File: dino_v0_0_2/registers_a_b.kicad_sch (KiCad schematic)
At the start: 21 parts, among them U31 74LS373, U32 74LS373, U33 74LS373, U35 74LS373, U41 74LS245, U42 74LS245, U43 74LS245, U44 74LS245, U5 74LS08, U57 74LS02

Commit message: feat(kicad): footprints, power sheet, global labels, PCB draft
Every symbol gets a stock THT footprint (plain DIP, no sockets, so the
3D render shows ICs). New Power sheet: 24-pin ATX header for a picoPSU,
rails +5V/+3.3V/+12V/-12V/GND only; no -5V exists on any ATX unit since
2003, none drawn. PS_ON# on a 2-pin header.

Cross-sheet labels become global labels. KiCad joined nothing between
sheets before: 122 base names were split per sheet, ERC saw 90 undriven
inputs whose driver sat one sheet away, and the PCB ratsnest stopped at
every sheet boundary. Proof: KiCad's netlist after equals a name-join of
its netlist before plus the 15 CW alias pairs, pin for pin.

kicad_contracts took a node's sheet from the net name's /Sheet/ prefix;
global nets have none, so it emitted an empty contracts doc. Sheet now
comes from the component's own path; the doc regenerates with zero diff.

ERC 477 -> 2. Real fixes: ROM I/O pins input -> tri_state, '382 GND pin
power_out -> power_in, four orphan symbols rehomed to project lib `dino`,
one stub wire. 133 by-design warnings excluded by uuid ('245 readback on
counter Q, alias stubs, probe-point labels); the two left are bus
signals the peripheral bus sheet will consume.

PCB draft: 198 footprints placed per sheet, all pads netted, no tracks.

Co-Authored-By: Claude Fable 5.1 <noreply@anthropic.com>
Claude-Session: https://claude.ai/code/session_018irreFHb1xEykW5kCD26ow
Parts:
- C38, C39, C40, C41, C42, C43, C44, C45, C46, C47, C64: footprint (none) -> Capacitor_THT:C_Disc_D5.0mm_W2.5mm_P2.50mm
- U31, U32, U33, U35, U41, U42, U43, U44: footprint (none) -> Package_DIP:DIP-20_W7.62mm
- U5, U57: footprint (none) -> Package_DIP:DIP-14_W7.62mm

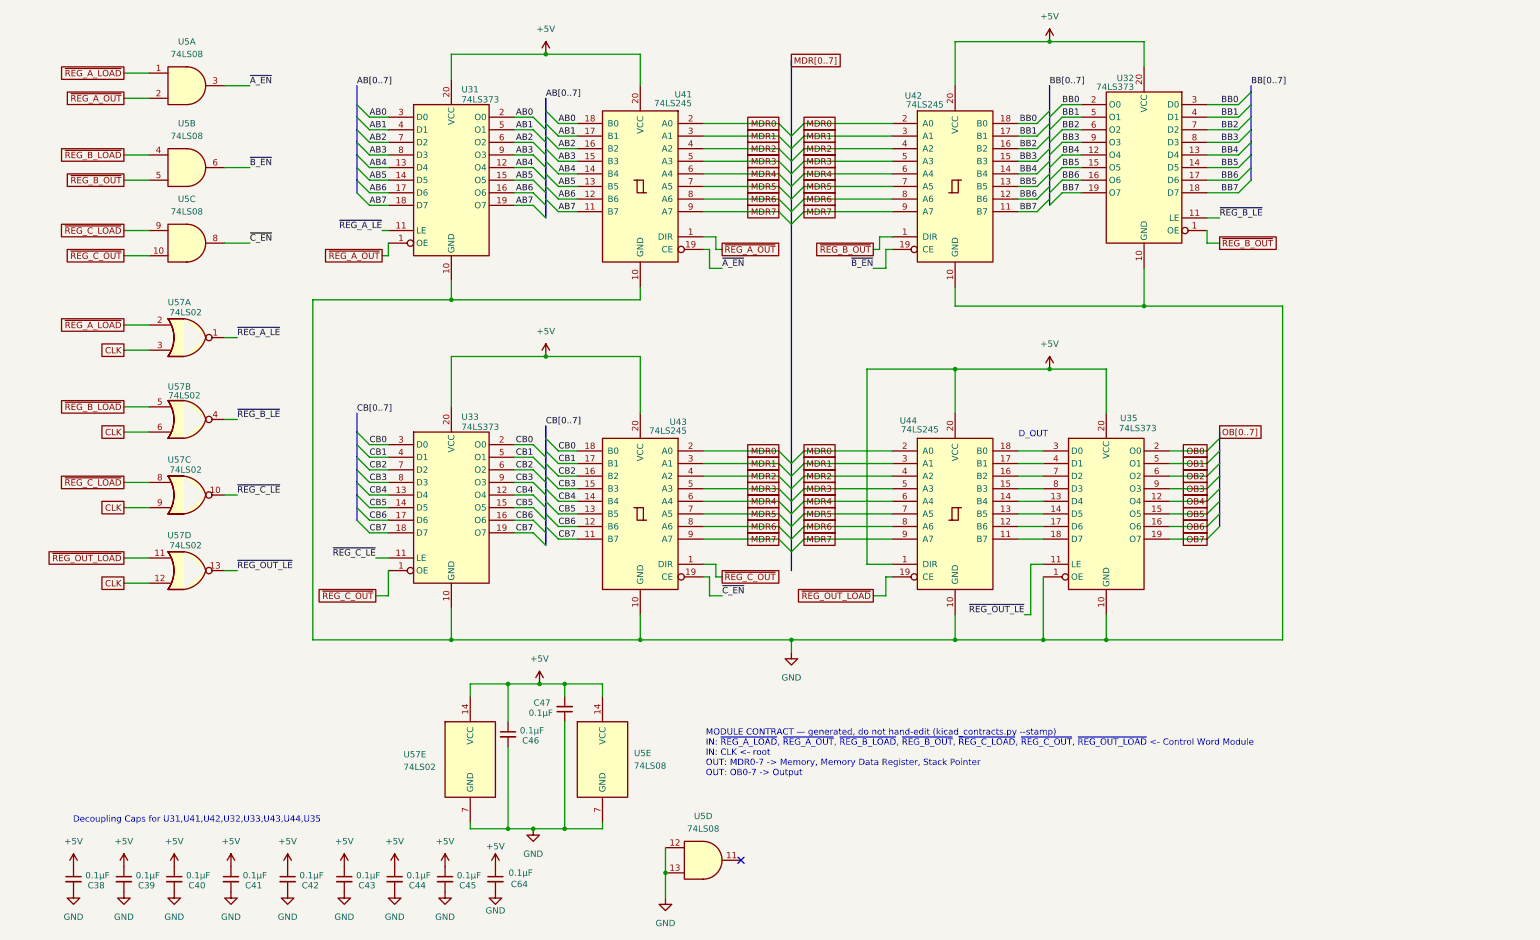
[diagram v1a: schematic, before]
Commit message: feat(int): draw the interrupt block; sheet cleanup pass
New sheet dino_v0_0_2/interrupt.kicad_sch (page 15): U80-U87, R28 4.7k
pull-up on ~{IRQ}, R29 100R on the block's CLK branch, C83-C90. Every
pin per PHASE_INT SECTION 3, checked against the plan with kicad_netlist
and kicad-cli (146 pins, 0 mismatches).

Old sheets (SECTION 3.2): U28.4 lifted off GND to INJECT; U61.3 to
END_OR_ACCEPT; U36.1 to PC_UP_GATED; U49 D0-3 cut from U48 Za-Zd and
routed through U87 as FLAG_NEXT0-3 / FLAG_D0-3; FLAG_C/Z/V/N and the
five decoder outputs made global. dino_serial: U104 74LS05, INTR ->
~{IRQ}, C4.

Placement pass on every sheet: bus entries and global labels no longer
share wires; M, CW, T, IRB and SA buses kept as labelled keys. Nets
diffed against HEAD per sheet: only the intended changes and a rotated
C29. Project ERC: 0 errors. MODULE CONTRACT stamps regenerated.

Co-Authored-By: Claude Fable 5.1 <noreply@anthropic.com>
Claude-Session: https://claude.ai/code/session_01JGxSS4MVUcaZdKZGtKroSg
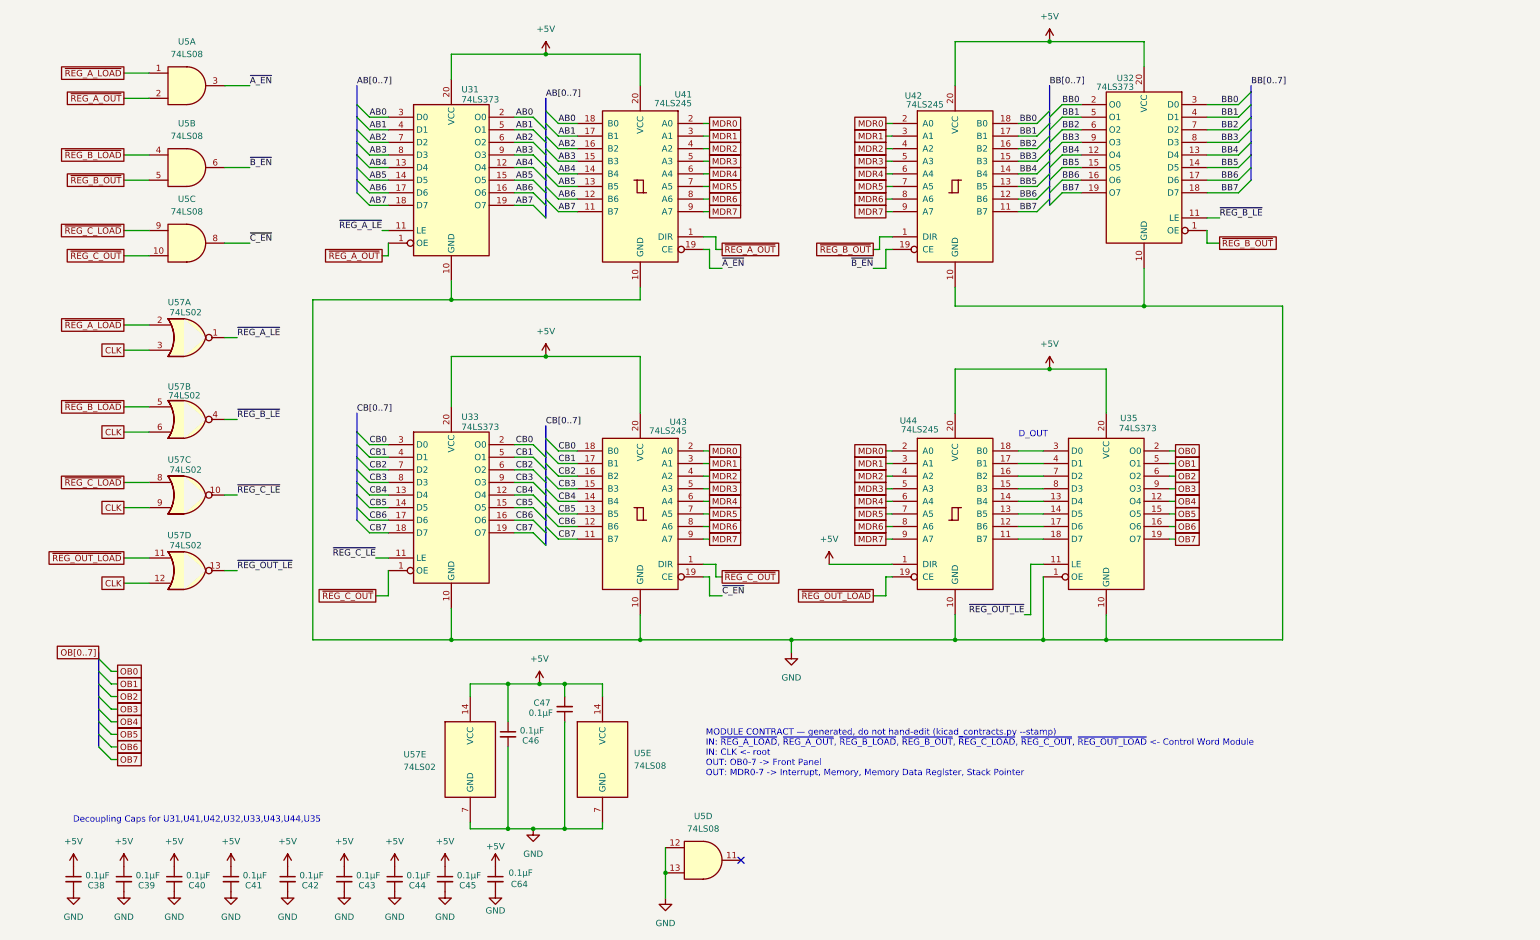
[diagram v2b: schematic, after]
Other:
- note added: "MODULE CONTRACT — generated, do not hand-edit (kicad_contracts.py --stamp) IN: ~{REG_A_LOAD}, ~{REG_A_OUT}, ~{REG_B_LOAD}, ~{REG_B_OUT}, ~{REG_C_LOAD}, ~{REG_C_OUT}, ~{REG_OUT_LOAD} <- Control Word Module IN: CLK <- root OUT: OB0-7 -> Front Panel OUT: MDR0-7 -> Interrupt, Memory, Memory Data Register, Stack Pointer"
- note removed: "MODULE CONTRACT — generated, do not hand-edit (kicad_contracts.py --stamp) IN: ~{REG_A_LOAD}, ~{REG_A_OUT}, ~{REG_B_LOAD}, ~{REG_B_OUT}, ~{REG_C_LOAD}, ~{REG_C_OUT}, ~{REG_OUT_LOAD} <- Control Word Module IN: CLK <- root OUT: MDR0-7 -> Memory, Memory Data Register, Stack Pointer OUT: OB0-7 -> Output"
